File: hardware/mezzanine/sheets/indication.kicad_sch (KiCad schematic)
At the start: 7 parts

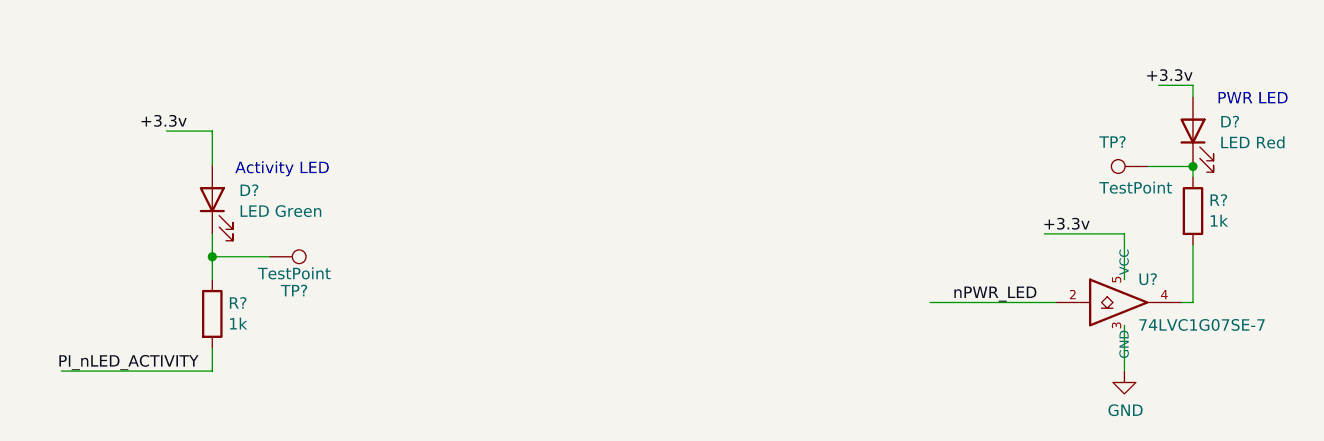
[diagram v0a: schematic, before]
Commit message: start routing mezzanine
making a progress capture before trying to cram a lot of signals onto just one hirose connector...
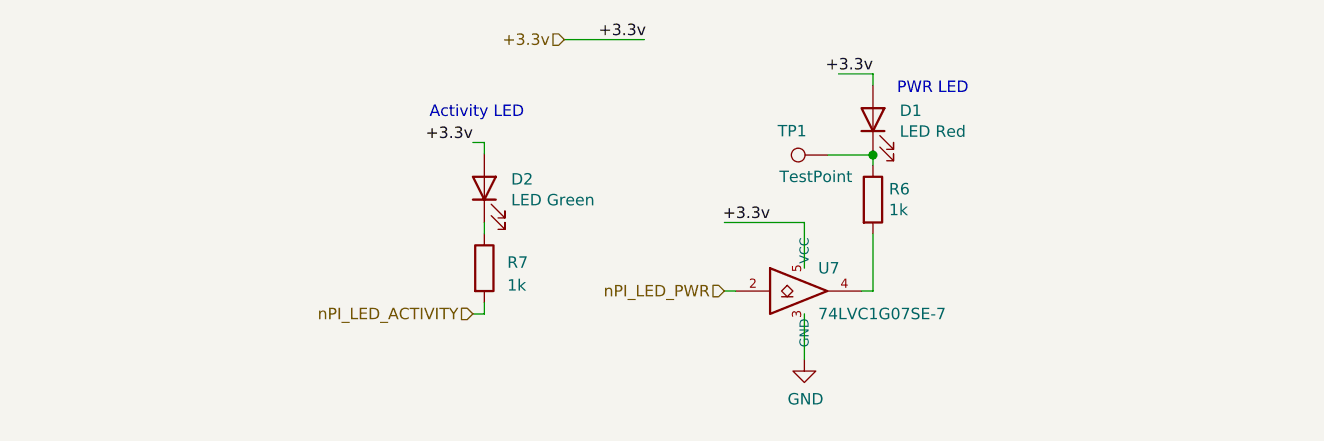
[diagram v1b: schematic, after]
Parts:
- removed D?: LED Green, LED_SMD:LED_0603_1608Metric, symbol Device:LED
- removed R?: 1k, Resistor_SMD:R_0402_1005Metric, symbol Device:R
- removed TP?: TestPoint, TestPoint:TestPoint_Pad_2.0x2.0mm, symbol Connector:TestPoint
- added D2: LED Green, LED_SMD:LED_0603_1608Metric, symbol Device:LED
- added R7: 1k, Resistor_SMD:R_0603_1608Metric, symbol Device:R
- gave numbers to parts that had none: 4
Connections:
- net +3.3v: now also D2.2 (A)
- net nPWR_LED renamed nPI_LED_PWR
- new net: D2.1 (K), R7.1
- new net nPI_LED_ACTIVITY: R7.2
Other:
- moved on the sheet: D1, R6, TP1, U7

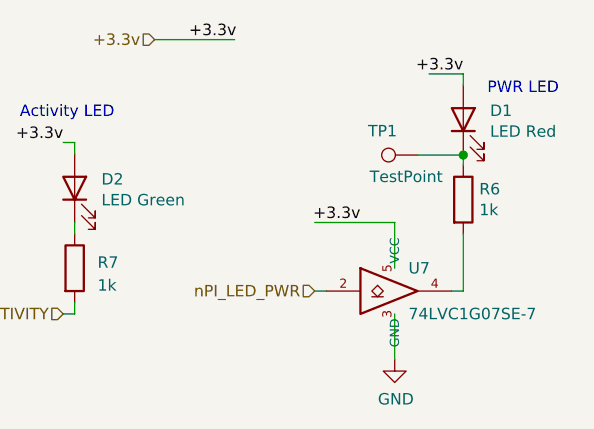
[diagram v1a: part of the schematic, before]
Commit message: finished mezzanine signal routing
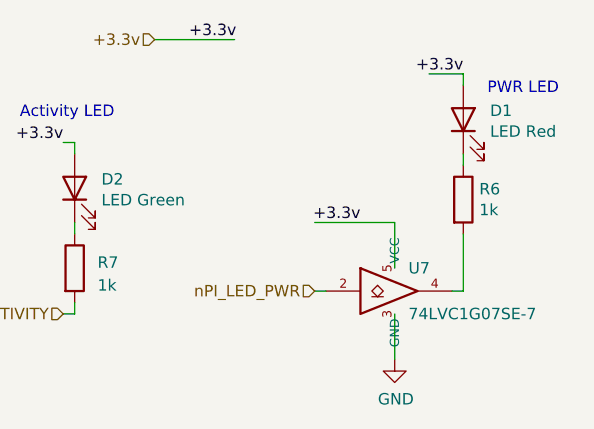
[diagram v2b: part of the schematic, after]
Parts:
- removed TP1: TestPoint, TestPoint:TestPoint_Pad_2.0x2.0mm, symbol Connector:TestPoint
- D1: Field4 Digikey -> (none); Field5 LTST-S270KRKT -> (none); Field6 SML-A12U8TT86Q -> (none); Field7 Rohm -> (none); Field8 650295101 -> (none); Part Description Red 620nm LED Indication - Discrete 2.2V 2-SMD, No Lead -> (none)
- D2: Field4 Digikey -> (none); Field5 LTST-S270KGKT -> (none); Field6 SML-A12M8TT86N -> (none); Field7 Rohm -> (none); Field8 650263301 -> (none); Part Description Green 572nm LED Indication - Discrete 2.2V 2-SMD, No Lead -> (none)
- R6: footprint Resistor_SMD:R_0402_1005Metric -> Resistor_SMD:R_0603_1608Metric; Field4 Farnell -> (none); Field5 9239235 -> (none); Field6 RK73H1ETTP1001F -> (none); Field7 KOA EUROPE GMBH -> (none); Field8 125049511 -> (none); Part Description Resistor 1K M1005 1% 63mW -> (none)
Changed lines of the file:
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@@
 (kicad_sch (version 20210406) (generator eeschema)
   (paper "A4")
-  (junction (at 173.99 77.597) (diameter 1.016) (color 0 0 0 0))
   (wire (pts (xy 129.54 76.2) (xy 130.81 76.2))
     (stroke (width 0) (type solid) (color 0 0 0 0))
@@
     (stroke (width 0) (type solid) (color 0 0 0 0))
   )
-  (wire (pts (xy 168.9862 77.597) (xy 173.99 77.597))
-    (stroke (width 0) (type solid) (color 0 0 0 0))
-  )
   (wire (pts (xy 173.99 68.58) (xy 170.18 68.58))
     (stroke (width 0) (type solid) (color 0 0 0 0))
@@
     (stroke (width 0) (type solid) (color 0 0 0 0))
   )
-  (wire (pts (xy 173.99 77.47) (xy 173.99 77.597))
-    (stroke (width 0) (type solid) (color 0 0 0 0))
-  )
-  (wire (pts (xy 173.99 77.597) (xy 173.99 78.74))
+  (wire (pts (xy 173.99 77.47) (xy 173.99 78.74))
     (stroke (width 0) (type solid) (color 0 0 0 0))
   )
@@
     (effects (font (size 1.27 1.27)) (justify right))
   )
-  (symbol (lib_id "Connector:TestPoint") (at 168.9862 77.597 90) (unit 1)
-    (in_bom yes) (on_board yes)
-    (property "Reference" "TP1" (id 0) (at 166.624 74.93 90)
-      (effects (font (size 1.27 1.27)) (justify left))
-    )
-    (property "Value" "TestPoint" (id 1) (at 171.704 80.01 90)
-      (effects (font (size 1.27 1.27)) (justify left))
-    )
-    (property "Footprint" "TestPoint:TestPoint_Pad_2.0x2.0mm" (id 2) (at 168.9862 72.517 0)
-      (effects (font (size 1.27 1.27)) hide)
-    )
-    (property "Datasheet" "" (id 3) (at 168.9862 72.517 0)
-      (effects (font (size 1.27 1.27)) hide)
-    )
-    (property "Field4" "nf" (id 4) (at 168.9862 77.597 0)
-      (effects (font (size 1.27 1.27)) hide)
-    )
-    (property "Field5" "nf" (id 5) (at 168.9862 77.597 0)
-      (effects (font (size 1.27 1.27)) hide)
-    )
-    (property "Field6" "nf" (id 6) (at 168.9862 77.597 0)
-      (effects (font (size 1.27 1.27)) hide)
-    )
-    (property "Field7" "nf" (id 7) (at 168.9862 77.597 0)
-      (effects (font (size 1.27 1.27)) hide)
-    )
-    (pin "1")
-  )
   (symbol (lib_id "power:GND") (at 166.37 100.33 0) (unit 1)
     (in_bom yes) (on_board yes)
-    (property "Reference" "#PWR077" (id 0) (at 166.37 106.68 0)
+    (property "Reference" "#PWR055" (id 0) (at 166.37 106.68 0)
       (effects (font (size 1.27 1.27)) hide)
     )
@@
       (effects (font (size 1.27 1.27)) (justify left))
     )
-    (property "Footprint" "Resistor_SMD:R_0402_1005Metric" (id 2) (at 172.212 82.55 90)
+    (property "Footprint" "Resistor_SMD:R_0603_1608Metric" (id 2) (at 172.212 82.55 90)
       (effects (font (size 1.27 1.27)) hide)
     )
-    (property "Datasheet" "https://fscdn.rohm.com/en/products/databook/datasheet/passive/resistor/chip_resistor/mcr-e.pdf" (id 3) (at 173.99 82.55 0)
-      (effects (font (size 1.27 1.27)) hide)
-    )
-    (property "Field4" "Farnell" (id 4) (at 173.99 82.55 0)
-      (effects (font (size 1.27 1.27)) hide)
-    )
-    (property "Field5" "9239235" (id 5) (at 173.99 82.55 0)
-      (effects (font (size 1.27 1.27)) hide)
-    )
-    (property "Field7" "KOA EUROPE GMBH" (id 6) (at 173.99 82.55 0)
-      (effects (font (size 1.27 1.27)) hide)
-    )
-    (property "Field6" "RK73H1ETTP1001F" (id 7) (at 173.99 82.55 0)
-      (effects (font (size 1.27 1.27)) hide)
-    )
-    (property "Part Description" "Resistor 1K M1005 1% 63mW" (id 8) (at 173.99 82.55 0)
-      (effects (font (size 1.27 1.27)) hide)
-    )
-    (property "Field8" "125049511" (id 9) (at 173.99 82.55 0)
+    (property "Datasheet" "~" (id 3) (at 173.99 82.55 0)
       (effects (font (size 1.27 1.27)) hide)
     )
@@
       (effects (font (size 1.27 1.27)) hide)
     )
-    (property "Datasheet" "http://optoelectronics.liteon.com/upload/download/DS22-2000-226/LTST-S270KGKT.pdf" (id 3) (at 130.81 81.28 0)
-      (effects (font (size 1.27 1.27)) hide)
-    )
-    (property "Field4" "Digikey " (id 4) (at 130.81 81.28 0)
-      (effects (font (size 1.27 1.27)) hide)
-    )
-    (property "Field5" "LTST-S270KGKT" (id 5) (at 130.81 81.28 0)
-      (effects (font (size 1.27 1.27)) hide)
-    )
-    (property "Field6" "SML-A12M8TT86N" (id 6) (at 130.81 81.28 0)
-      (effects (font (size 1.27 1.27)) hide)
-    )
-    (property "Field7" "Rohm" (id 7) (at 130.81 81.28 0)
-      (effects (font (size 1.27 1.27)) hide)
-    )
-    (property "Field8" "650263301" (id 8) (at 130.81 81.28 0)
-      (effects (font (size 1.27 1.27)) hide)
-    )
-    (property "Part Description" "Green 572nm LED Indication - Discrete 2.2V 2-SMD, No Lead" (id 9) (at 130.81 81.28 0)
+    (property "Datasheet" "~" (id 3) (at 130.81 81.28 0)
       (effects (font (size 1.27 1.27)) hide)
     )
@@
       (effects (font (size 1.27 1.27)) hide)
     )
-    (property "Datasheet" "http://optoelectronics.liteon.com/upload/download/DS22-2000-210/LTST-S270KRKT.pdf" (id 3) (at 173.99 73.66 0)
+    (property "Datasheet" "~" (id 3) (at 173.99 73.66 0)
       (effects (font (size 1.27 1.27)) hide)
     )
-    (property "Field4" "Digikey " (id 4) (at 173.99 73.66 0)
-      (effects (font (size 1.27 1.27)) hide)
-    )
-    (property "Field5" "	LTST-S270KRKT" (id 5) (at 173.99 73.66 0)
-      (effects (font (size 1.27 1.27)) hide)
-    )
-    (property "Field6" "SML-A12U8TT86Q" (id 6) (at 173.99 73.66 0)
-      (effects (font (size 1.27 1.27)) hide)
-    )
-    (property "Field7" "Rohm" (id 7) (at 173.99 73.66 0)
-      (effects (font (size 1.27 1.27)) hide)
-    )
-    (property "Field8" "650295101" (id 8) (at 173.99 73.66 0)
-      (effects (font (size 1.27 1.27)) hide)
-    )
-    (property "Part Description" "	Red 620nm LED Indication - Discrete 2.2V 2-SMD, No Lead" (id 9) (at 173.99 73.66 0)
-      (effects (font (size 1.27 1.27)) hide)
-    )

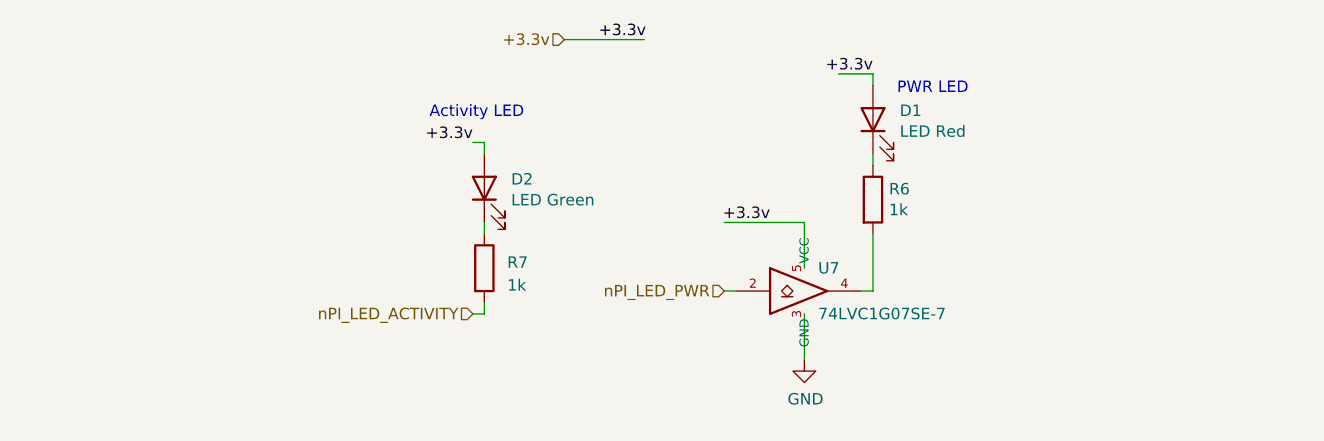
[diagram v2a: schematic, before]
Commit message: sheet refs relative, copied escalator pinout to lobby
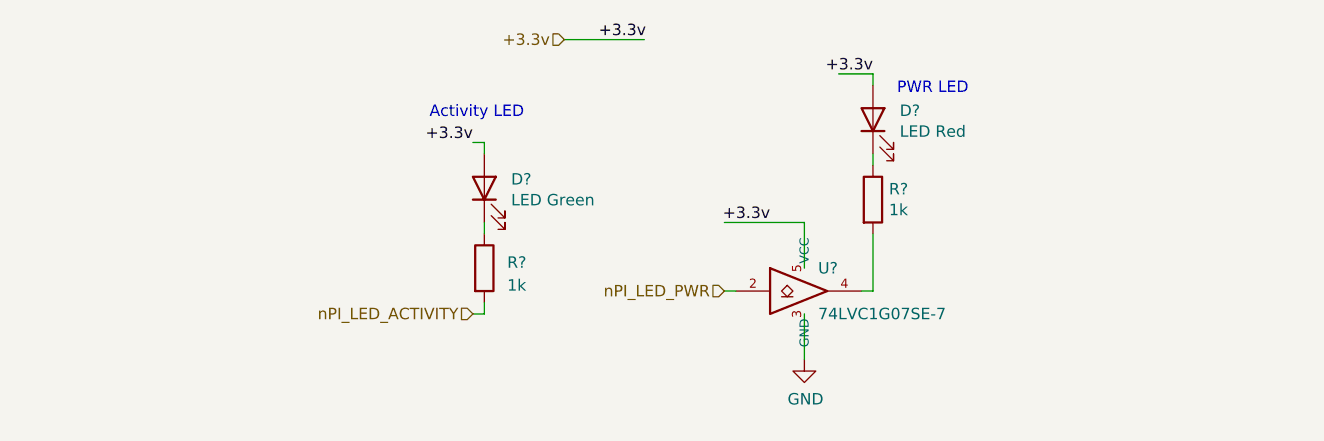
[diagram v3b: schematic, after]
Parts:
- renumbered D1 to D?, D2 to D?, R7 to R?, R6 to R?, U7 to U?
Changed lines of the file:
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@@
   (symbol (lib_id "power:GND") (at 166.37 100.33 0) (unit 1)
     (in_bom yes) (on_board yes)
-    (property "Reference" "#PWR055" (id 0) (at 166.37 106.68 0)
+    (property "Reference" "#PWR?" (id 0) (at 166.37 106.68 0)
       (effects (font (size 1.27 1.27)) hide)
     )
@@
   (symbol (lib_id "Device:R") (at 130.81 90.17 0) (unit 1)
     (in_bom yes) (on_board yes) (fields_autoplaced)
-    (property "Reference" "R7" (id 0) (at 133.35 89.5349 0)
+    (property "Reference" "R?" (id 0) (at 133.35 89.5349 0)
       (effects (font (size 1.27 1.27)) (justify left))
     )
@@
   (symbol (lib_id "Device:R") (at 173.99 82.55 0) (unit 1)
     (in_bom yes) (on_board yes)
-    (property "Reference" "R6" (id 0) (at 175.768 81.3816 0)
+    (property "Reference" "R?" (id 0) (at 175.768 81.3816 0)
       (effects (font (size 1.27 1.27)) (justify left))
     )
@@
   (symbol (lib_id "Device:LED") (at 130.81 81.28 90) (unit 1)
     (in_bom yes) (on_board yes)
-    (property "Reference" "D2" (id 0) (at 133.7818 80.2894 90)
+    (property "Reference" "D?" (id 0) (at 133.7818 80.2894 90)
       (effects (font (size 1.27 1.27)) (justify right))
     )
@@
   (symbol (lib_id "Device:LED") (at 173.99 73.66 90) (unit 1)
     (in_bom yes) (on_board yes)
-    (property "Reference" "D1" (id 0) (at 176.9618 72.6694 90)
+    (property "Reference" "D?" (id 0) (at 176.9618 72.6694 90)
       (effects (font (size 1.27 1.27)) (justify right))
     )
@@
   (symbol (lib_id "CM4IO:74LVC1G07_copy") (at 166.37 92.71 0) (unit 1)
     (in_bom yes) (on_board yes)
-    (property "Reference" "U7" (id 0) (at 167.894 90.17 0)
+    (property "Reference" "U?" (id 0) (at 167.894 90.17 0)
       (effects (font (size 1.27 1.27)) (justify left))
     )

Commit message: addtl hdmi routing
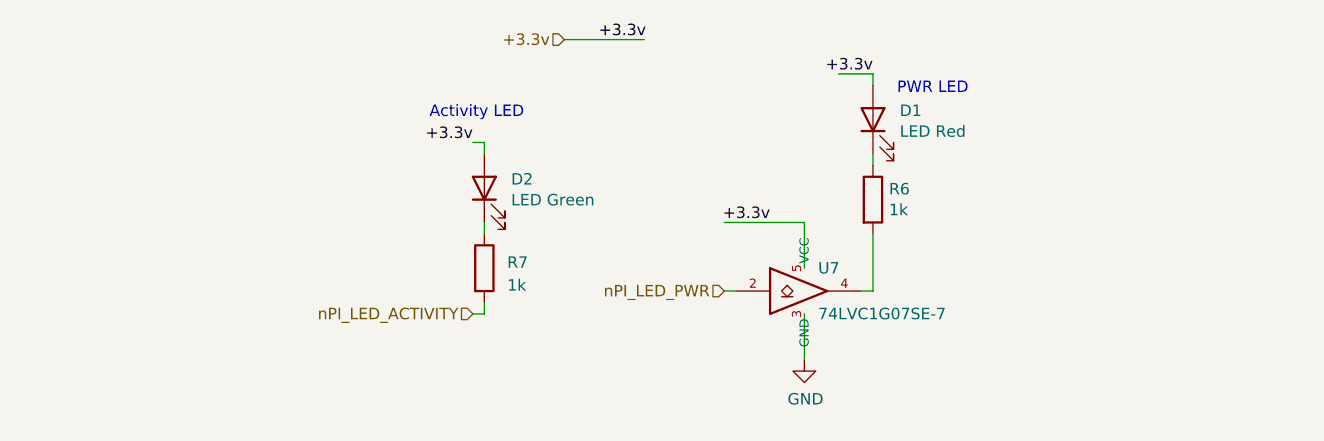
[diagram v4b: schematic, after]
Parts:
- gave numbers to parts that had none: 5
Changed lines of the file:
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@@
   (symbol (lib_id "power:GND") (at 166.37 100.33 0) (unit 1)
     (in_bom yes) (on_board yes)
-    (property "Reference" "#PWR?" (id 0) (at 166.37 106.68 0)
+    (property "Reference" "#PWR0125" (id 0) (at 166.37 106.68 0)
       (effects (font (size 1.27 1.27)) hide)
     )
@@
   (symbol (lib_id "Device:R") (at 130.81 90.17 0) (unit 1)
     (in_bom yes) (on_board yes) (fields_autoplaced)
-    (property "Reference" "R?" (id 0) (at 133.35 89.5349 0)
+    (property "Reference" "R7" (id 0) (at 133.35 89.5349 0)
       (effects (font (size 1.27 1.27)) (justify left))
     )
@@
   (symbol (lib_id "Device:R") (at 173.99 82.55 0) (unit 1)
     (in_bom yes) (on_board yes)
-    (property "Reference" "R?" (id 0) (at 175.768 81.3816 0)
+    (property "Reference" "R6" (id 0) (at 175.768 81.3816 0)
       (effects (font (size 1.27 1.27)) (justify left))
     )
@@
   (symbol (lib_id "Device:LED") (at 130.81 81.28 90) (unit 1)
     (in_bom yes) (on_board yes)
-    (property "Reference" "D?" (id 0) (at 133.7818 80.2894 90)
+    (property "Reference" "D2" (id 0) (at 133.7818 80.2894 90)
       (effects (font (size 1.27 1.27)) (justify right))
     )
@@
   (symbol (lib_id "Device:LED") (at 173.99 73.66 90) (unit 1)
     (in_bom yes) (on_board yes)
-    (property "Reference" "D?" (id 0) (at 176.9618 72.6694 90)
+    (property "Reference" "D1" (id 0) (at 176.9618 72.6694 90)
       (effects (font (size 1.27 1.27)) (justify right))
     )
@@
   (symbol (lib_id "CM4IO:74LVC1G07_copy") (at 166.37 92.71 0) (unit 1)
     (in_bom yes) (on_board yes)
-    (property "Reference" "U?" (id 0) (at 167.894 90.17 0)
+    (property "Reference" "U7" (id 0) (at 167.894 90.17 0)
       (effects (font (size 1.27 1.27)) (justify left))
     )
